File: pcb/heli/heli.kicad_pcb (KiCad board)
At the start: 4 copper layers, 50.6 x 50 mm, 74 parts, among them J1 Batterie, J2 Debug, J3 CONMHF4-SMD-G-T, J4 Servo, J5 Servo, M1 Motor_DC, M2 Motor_DC, Q2 BC547, Q3 IRLZ44N, Q4 BC547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

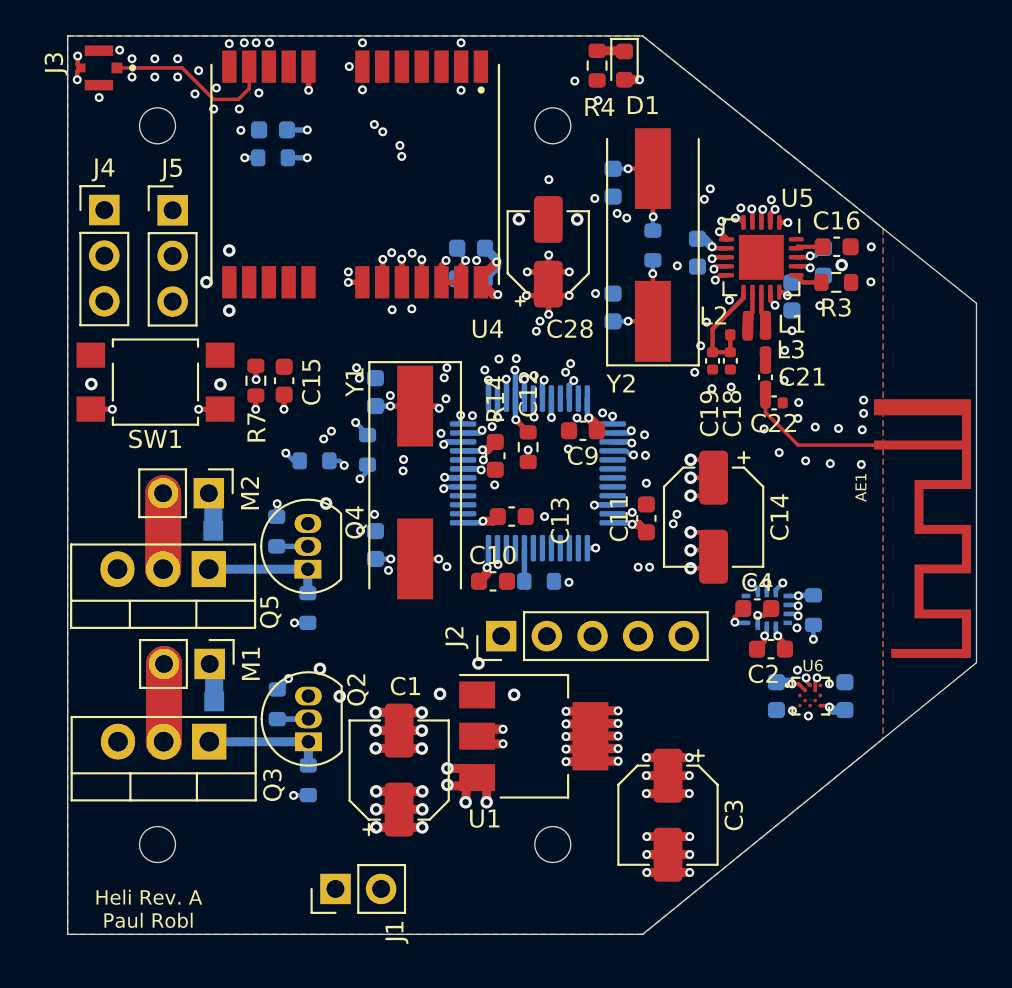
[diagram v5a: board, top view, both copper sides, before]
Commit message: 
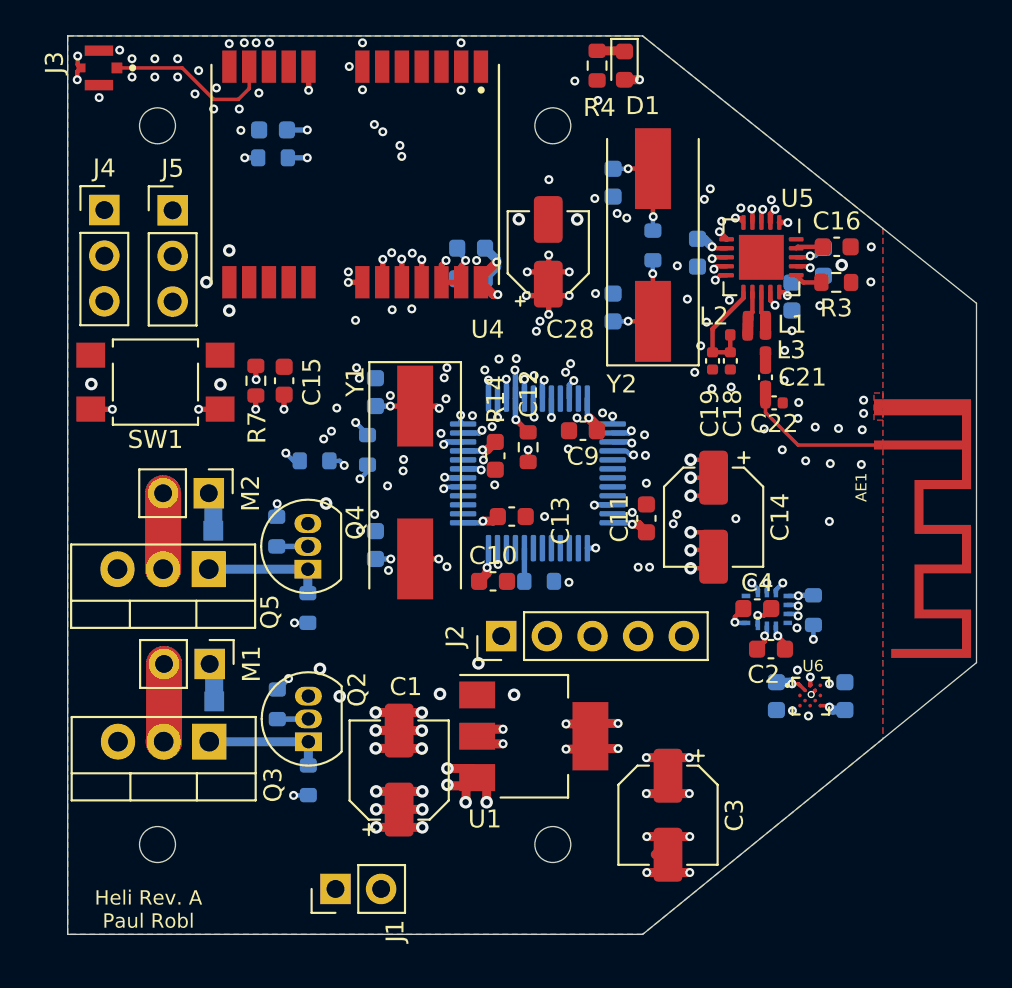
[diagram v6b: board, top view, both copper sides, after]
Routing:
- net 3.3V: track 60.3 -> 52.3 mm, vias 48 -> 46
- net GND: track 27.3 -> 25.7 mm, vias 143 -> 141
- net /IMU/SDA: track 7.13 -> 7.78 mm
